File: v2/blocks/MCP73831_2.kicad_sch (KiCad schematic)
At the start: 6 parts, among them U5 MCP73831T-2ACI/OT

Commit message: routing done
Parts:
- renumbered R18 to R15
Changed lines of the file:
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@@
 		(dnp no)
 		(fields_autoplaced yes)
-		(property "Reference" "R18"
+		(property "Reference" "R15"
 			(at 78.74 62.23 0)
 			(effects
@@
 			(project ""
 				(path "/61d36b12-c329-4dd2-b08b-b63678fc7b25/b43a13e0-fb46-41c2-b610-4837c97a9ae2"
-					(reference "R18")
+					(reference "R15")
 					(unit 1)
 				)
@@
 				)
 				(path "/61d36b12-c329-4dd2-b08b-b63678fc7b25/b43a13e0-fb46-41c2-b610-4837c97a9ae2"
-					(reference "R19")
-					(unit 1)
-				)
+					(reference "R16")
+					(unit 1)
+				)

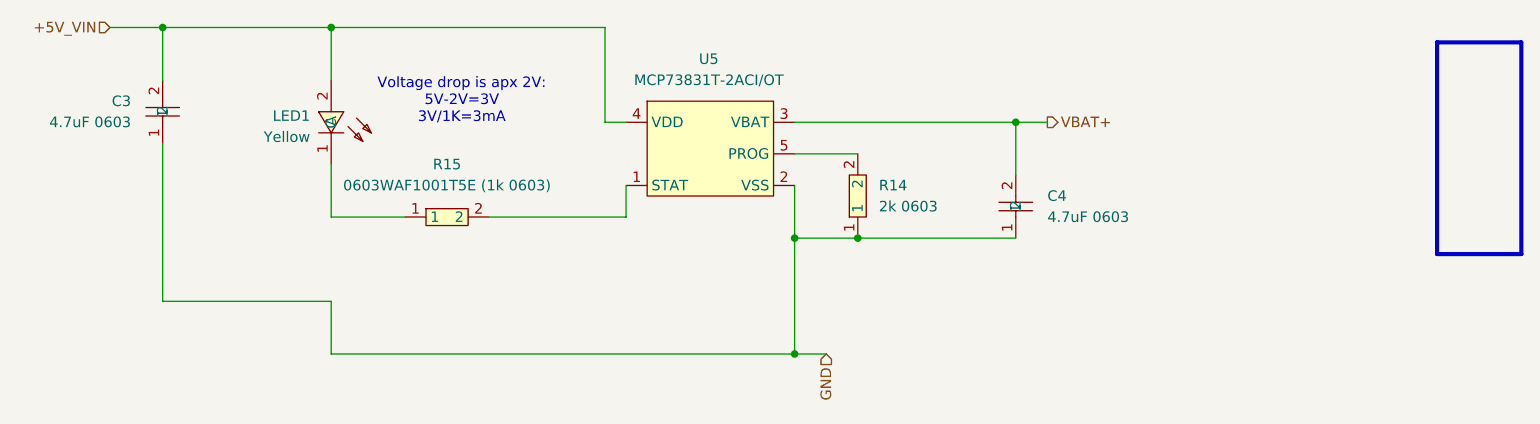
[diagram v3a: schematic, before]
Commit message: can transceiver and battery reverse polarity bypass
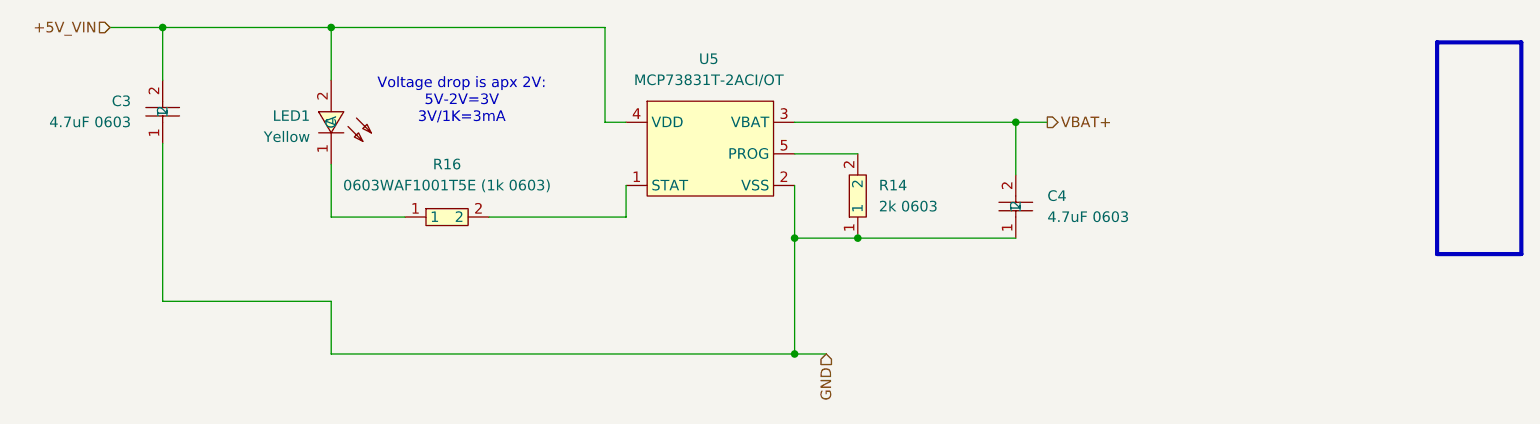
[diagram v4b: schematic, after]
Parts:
- renumbered R15 to R16
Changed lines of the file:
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@@
 		(shape input)
 		(at 38.1 45.72 180)
+		(fields_autoplaced yes)
 		(effects
 			(font
@@
 		(shape output)
 		(at 151.13 57.15 0)
+		(fields_autoplaced yes)
 		(effects
 			(font
@@
 		(shape input)
 		(at 124.46 85.09 270)
+		(fields_autoplaced yes)
 		(effects
 			(font
@@
 		(dnp no)
 		(fields_autoplaced yes)
-		(property "Reference" "R15"
+		(property "Reference" "R16"
 			(at 78.74 62.23 0)
 			(effects
@@
 			(project ""
 				(path "/61d36b12-c329-4dd2-b08b-b63678fc7b25/b43a13e0-fb46-41c2-b610-4837c97a9ae2"
-					(reference "R15")
+					(reference "R16")
 					(unit 1)
 				)
@@
 				)
 				(path "/61d36b12-c329-4dd2-b08b-b63678fc7b25/b43a13e0-fb46-41c2-b610-4837c97a9ae2"
-					(reference "R16")
-					(unit 1)
-				)
+					(reference "R17")
+					(unit 1)
+				)
